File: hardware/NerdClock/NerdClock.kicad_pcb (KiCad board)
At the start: 2 copper layers, 123 x 123 mm, 95 parts, among them J1 Conn_01x02, J10 Conn_01x04, J11 Conn_01x02, J12 Conn_01x02, J2 Jack-DC, J3 ICSP, J4 Conn_01x04, J5 Conn_01x02, J6 Conn_01x02, J7 USB_B_Micro, J8 Conn_01x02, J9 Conn_01x05, Q1 RTR025N03FRATL, Q2 RTR025N03FRATL, SW1 SW_MEC_5G, SW2 SW_MEC_5G, SW3 SW_MEC_5G, SW4 SW_MEC_5G, U1 IFX1117, U2 DRV8313, U3 ATmega168P-20AU, U4 DS1338Z-18+, U5 OPB706A, U6 CH340C, Y1 16MHz, Y2 32.768kHz/12.5pf

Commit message: Routing probably done?
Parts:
- added G***: LOGO, logo:oshw, F.Cu at (120.7, 71.6)
- moved SW1 20.0 mm to (65.0, 100.0)
- moved SW3 20.0 mm to (65.0, 80.0)
- moved R1 13.5 mm to (101.5, 61.0)
- moved Q2 1.95 mm to (94.5, 125.8), turned to 0 degrees
- moved R3 1.50 mm to (103.0, 66.5), turned to 180 degrees
- moved R2 1.08 mm to (97.0, 66.5)
- moved J3 0.79 mm to (141.4, 111.5)
- moved C10 0.75 mm to (135.1, 107.0)
- moved C13 0.75 mm to (124.2, 136.1)
- moved C6 0.75 mm to (135.1, 109.1)
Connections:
- U3 pad 24: SW3 -> Net-(U3-Pad24)
- U3 pad 26: Net-(U3-Pad26) -> SW3
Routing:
- net SW1: track 0.00 -> 122.8 mm, vias 0 -> 2
- net SW2: track 0.00 -> 109.3 mm, vias 0 -> 4
- net SW3: track 0.00 -> 101.6 mm, vias 0 -> 4
- net GND: track 9.30 -> 110.8 mm, vias 5 -> 103
- net +3V3: track 185.8 -> 272.4 mm, vias 8 -> 13
- net LED: track 24.2 -> 87.7 mm, vias 0 -> 2
- net DOT: track 0.00 -> 51.9 mm
- net VCC: track 177.0 -> 184.8 mm
- net SDA: track 66.9 -> 60.9 mm
- net nCPU_RESET: track 38.3 -> 44.0 mm
- net Net-(J3-Pad3): track 11.2 -> 15.6 mm
- net Net-(C10-Pad2): track 0.00 -> 4.09 mm
- net Net-(J12-Pad2): track 0.00 -> 3.38 mm
- net Net-(D1-Pad1): track 46.7 -> 49.5 mm
- net Net-(Q1-Pad1): track 0.00 -> 1.81 mm
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- added copper zone on B.Cu, net GND
- added copper zone on F.Cu, net GND
- removed copper zone on B.Cu, net Net-(J9-Pad5)
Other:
- board text added: "NerdClock 2127A © Tom Wimmenhove"

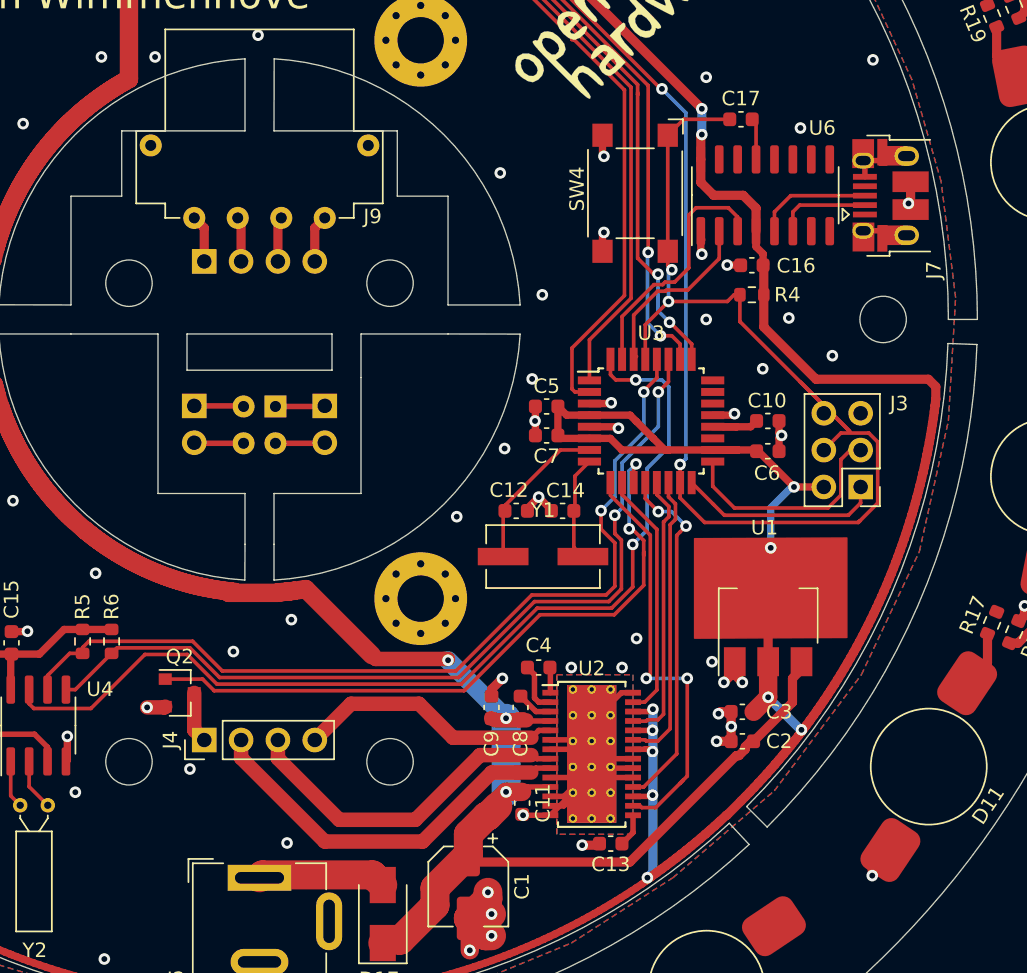
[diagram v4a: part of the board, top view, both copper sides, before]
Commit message: Fix all DRC errors
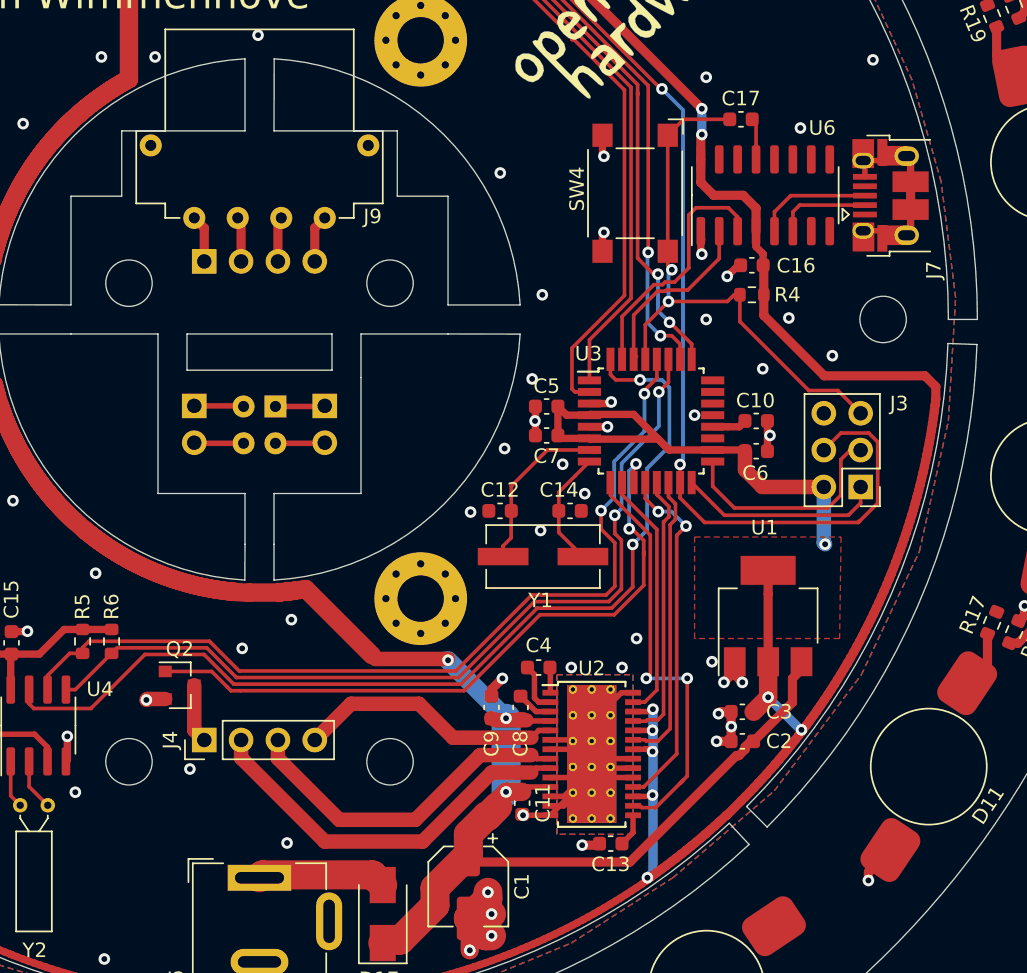
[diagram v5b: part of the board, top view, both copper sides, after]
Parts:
- moved C12 1.11 mm to (116.6, 113.2), turned to 180 degrees
- moved C10 0.80 mm to (134.2, 107.0)
- moved C6 0.80 mm to (134.2, 109.1)
- moved Q2 0.53 mm to (94.5, 125.2)
- moved C14 0.51 mm to (121.4, 113.2), turned to 0 degrees
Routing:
- net nCPU_RESET: track 44.0 -> 39.4 mm
- net +3V3: track 272.4 -> 269.5 mm, vias 13 -> 12
- net Net-(C10-Pad2): track 4.09 -> 2.39 mm
- net Net-(C14-Pad1): track 7.25 -> 8.11 mm
- net GND: track 110.8 -> 110.1 mm, vias 103 -> 104
- net VCC: track 184.8 -> 184.2 mm
- net Net-(J4-Pad1): track 3.54 -> 4.06 mm
- net Net-(C12-Pad1): track 11.0 -> 11.5 mm
- added copper zone on F.Cu, net +3V3

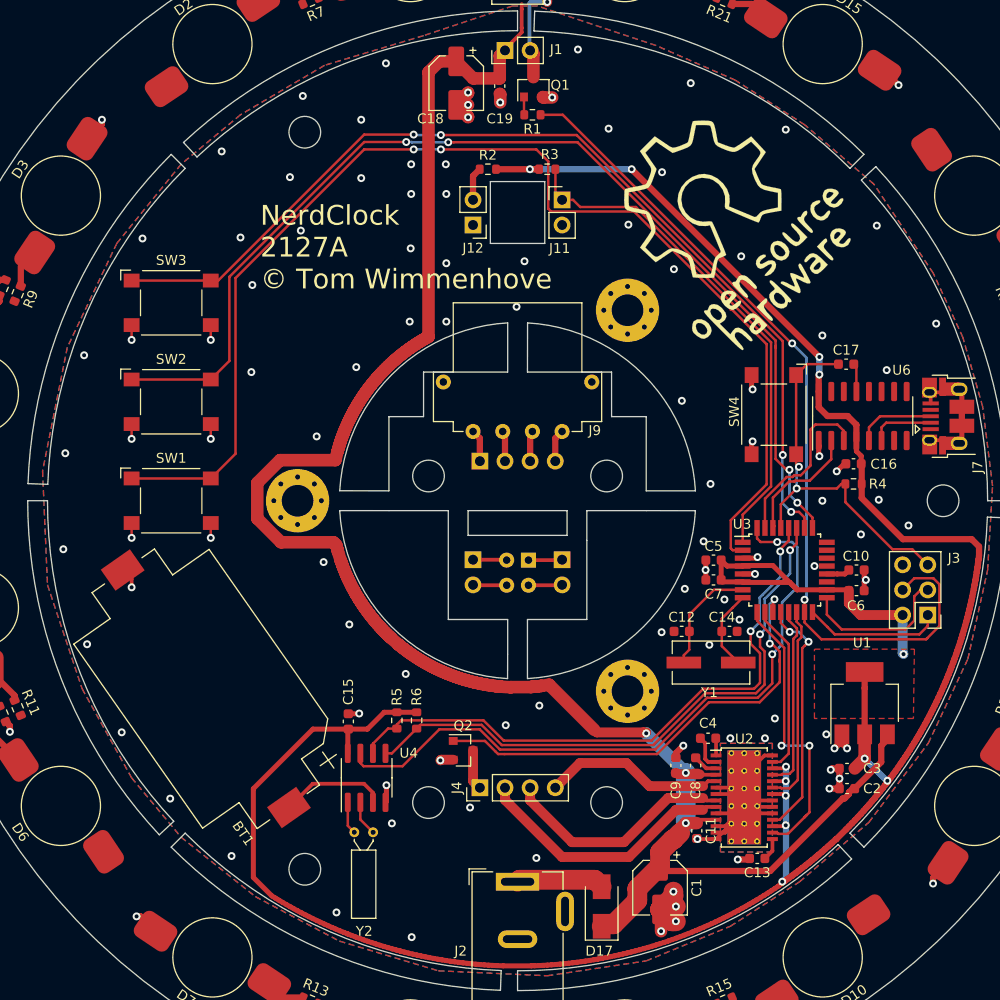
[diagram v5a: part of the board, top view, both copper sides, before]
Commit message: Removed excessive vias and change battery angle
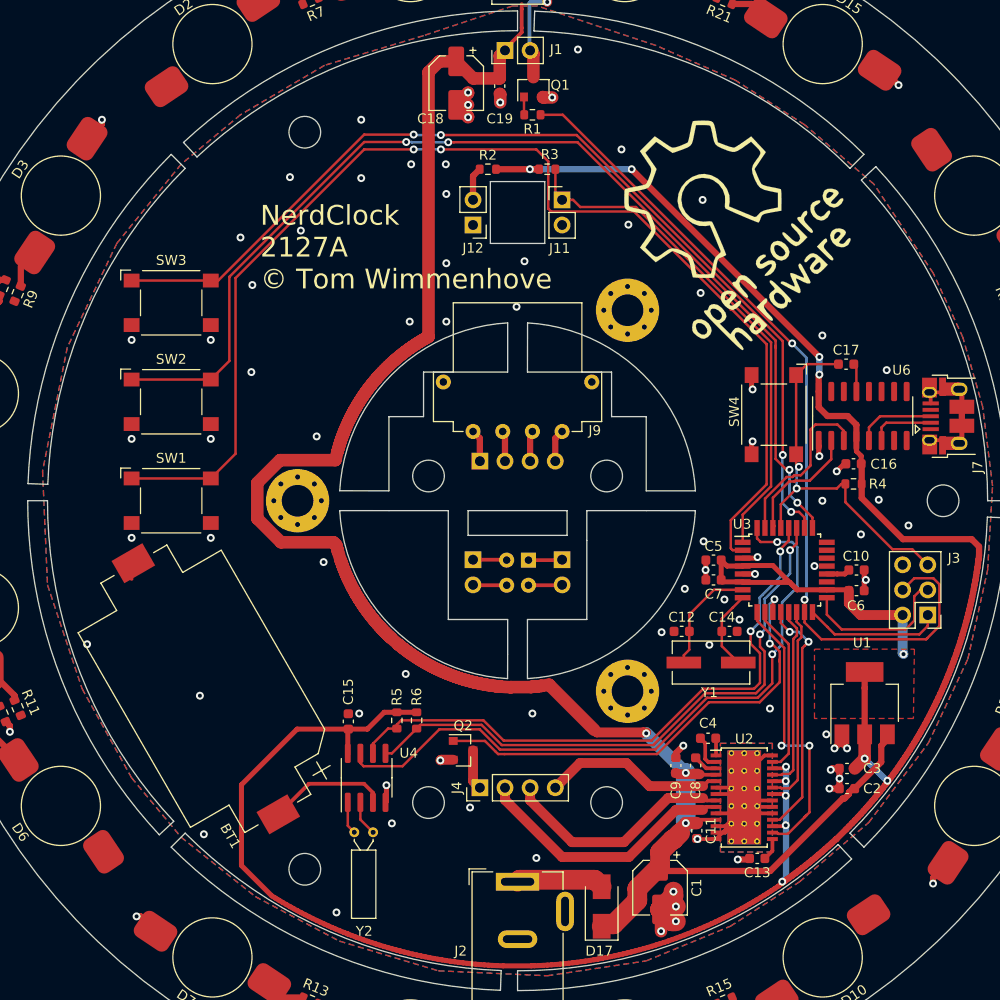
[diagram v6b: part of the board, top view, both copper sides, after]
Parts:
- turned BT1 to 120 degrees
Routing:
- net GND: track 110.1 -> 99.1 mm, vias 104 -> 80
- net +3V3: track 269.5 -> 271.4 mm
- net Net-(BT1-Pad1): track 10.8 -> 12.2 mm

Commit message: Added untested RTC code
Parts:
- added D18: LED, WhiteLed1W:WhiteLed1W, B.Cu at (91.0, 60.0)
- added D19: LED, WhiteLed1W:WhiteLed1W, B.Cu at (109.0, 60.0)
- added R23: 22R, Resistor_SMD:R_0603_1608Metric, B.Cu at (99.8, 57.9)
- added R24: 22R, Resistor_SMD:R_0603_1608Metric, B.Cu at (98.2, 57.9)
- moved R1 2.59 mm to (103.8, 62.2)
- moved Q1 1.52 mm to (102.2, 59.6), turned to 0 degrees
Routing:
- net Net-(D1-Pad1): track 50.0 -> 77.3 mm
- net VCC: track 184.2 -> 204.2 mm, vias 3 -> 4
- net GND: track 99.1 -> 92.6 mm, vias 80 -> 79
- net Net-(D19-Pad2): track 0.00 -> 4.02 mm
- net Net-(D18-Pad1): track 0.00 -> 2.67 mm
- net LED: track 87.5 -> 84.9 mm
- net Net-(Q1-Pad1): track 1.81 -> 4.29 mm
- net SW3: track 101.6 -> 100.5 mm
- net SW1: track 122.8 -> 122.1 mm
- net SW2: track 109.3 -> 108.6 mm

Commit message: Off to JLCPCB!
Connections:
- U2 pad 22: +3V3 -> EN_MOT
- U2 pad 24: +3V3 -> EN_MOT
- U2 pad 26: +3V3 -> EN_MOT
- U3 pad 23: Net-(U3-Pad23) -> EN_MOT
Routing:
- net EN_MOT: track 0.00 -> 35.7 mm, vias 0 -> 5
- net +3V3: track 271.4 -> 261.0 mm, vias 12 -> 9
- net nMOTOR_RESET: track 29.3 -> 30.2 mm
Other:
- board text added: "BOTTOM"
- board text added: "TOP"
